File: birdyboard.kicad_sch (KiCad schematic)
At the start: 5 parts, among them SW1 SW_SPST

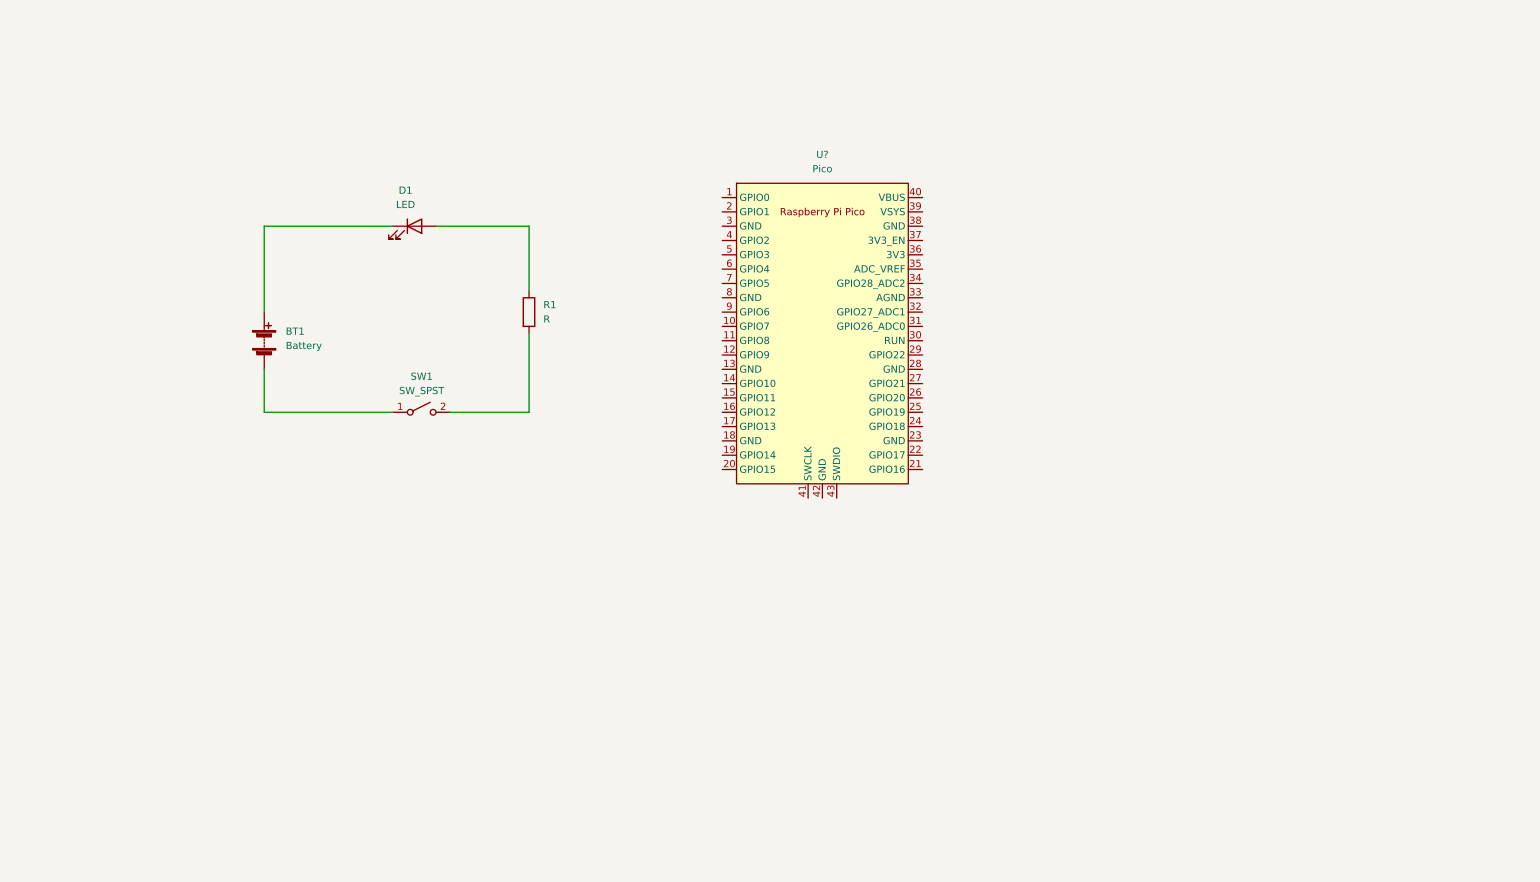
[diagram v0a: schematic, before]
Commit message: Adds footprints & symbols for RP2040 & TMC2208 boards
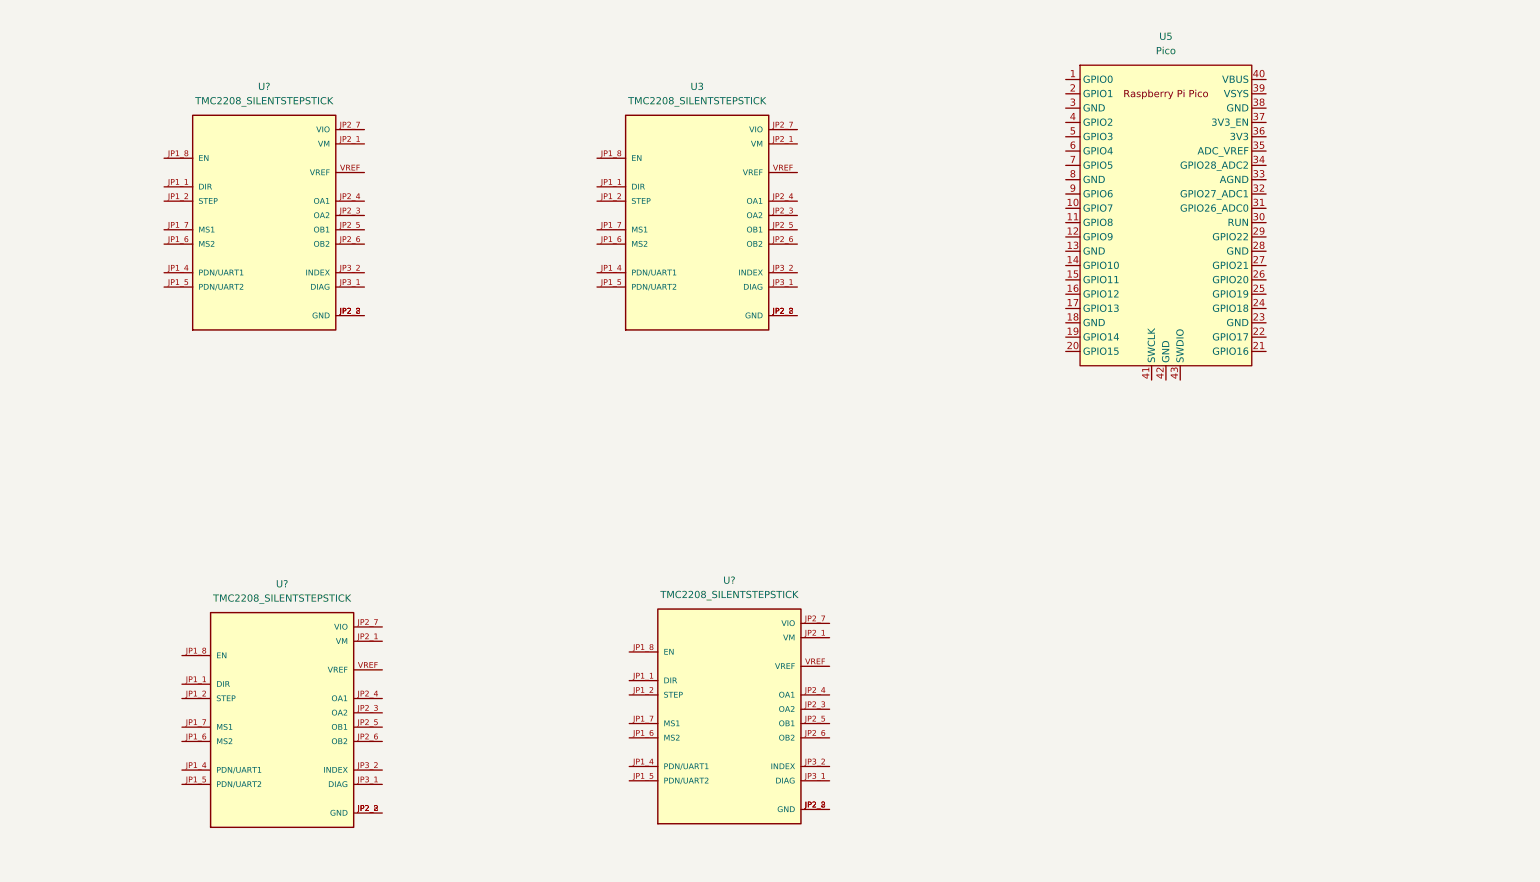
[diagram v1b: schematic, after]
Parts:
- removed BT1: Battery, symbol Device:Battery
- removed D1: LED, symbol Device:LED
- removed R1: R, symbol Device:R
- removed SW1: SW_SPST, symbol Switch:SW_SPST
- added U3, U? (x3): TMC2208_SILENTSTEPSTICK, birdyboard:TMC2208_SILENTSTEPSTICK, symbol birdyboard_library:TMC2208_SILENTSTEPSTICK
- U5: renamed from U?; footprint RPi_Pico:RPi_Pico_SMD_TH -> MCU_RaspberryPi_and_Boards:RPi_Pico_SMD_TH; symbol MCU_RaspberryPi_and_Boards:Pico -> birdyboard_library:Pico
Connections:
- new net: U3.JP2_2 (GND), U3.JP2_8 (GND)
- new net: U?.JP2_2 (GND), U?.JP2_8 (GND) (x3)
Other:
- moved on the sheet: U5
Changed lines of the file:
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@@
 (kicad_sch (version 20211123) (generator eeschema)
   (paper "A4")
-  (wire (pts (xy 109.22 60.96) (xy 109.22 72.39))
-    (stroke (width 0) (type default) (color 0 0 0 0))
-  )
-  (wire (pts (xy 109.22 80.01) (xy 109.22 93.98))
-    (stroke (width 0) (type default) (color 0 0 0 0))
-  )
-  (wire (pts (xy 62.23 93.98) (xy 62.23 86.36))
-    (stroke (width 0) (type default) (color 0 0 0 0))
-  )
-  (wire (pts (xy 109.22 93.98) (xy 95.25 93.98))
-    (stroke (width 0) (type default) (color 0 0 0 0))
-  )
-  (wire (pts (xy 62.23 60.96) (xy 85.09 60.96))
-    (stroke (width 0) (type default) (color 0 0 0 0))
-  )
-  (wire (pts (xy 92.71 60.96) (xy 109.22 60.96))
-    (stroke (width 0) (type default) (color 0 0 0 0))
-  )
-  (wire (pts (xy 62.23 76.2) (xy 62.23 60.96))
-    (stroke (width 0) (type default) (color 0 0 0 0))
-  )
-  (wire (pts (xy 85.09 93.98) (xy 62.23 93.98))
-    (stroke (width 0) (type default) (color 0 0 0 0))
-  )
-  (symbol (lib_id "Device:R") (at 109.22 76.2 0) (unit 1)
-    (in_bom yes) (on_board yes) (fields_autoplaced)
-    (property "Reference" "R1" (id 0) (at 111.76 74.9299 0)
-      (effects (font (size 1.27 1.27)) (justify left))
-    )
-    (property "Value" "R" (id 1) (at 111.76 77.4699 0)
-      (effects (font (size 1.27 1.27)) (justify left))
-    )
-    (property "Footprint" "" (id 2) (at 107.442 76.2 90)
+  (symbol (lib_id "birdyboard_library:TMC2208_SILENTSTEPSTICK") (at 139.065 59.055 0) (unit 1)
+    (in_bom yes) (on_board yes) (fields_autoplaced)
+    (property "Reference" "U3" (id 0) (at 139.065 36.195 0))
+    (property "Value" "TMC2208_SILENTSTEPSTICK" (id 1) (at 139.065 38.735 0))
+    (property "Footprint" "birdyboard:TMC2208_SILENTSTEPSTICK" (id 2) (at 139.065 59.055 0)
+      (effects (font (size 1.27 1.27)) (justify left bottom) hide)
+    )
+    (property "Datasheet" "" (id 3) (at 139.065 59.055 0)
+      (effects (font (size 1.27 1.27)) (justify left bottom) hide)
+    )
+    (property "MANUFACTURER" "Trinamic Motion" (id 4) (at 139.065 59.055 0)
+      (effects (font (size 1.27 1.27)) (justify left bottom) hide)
+    )
+    (pin "JP1_1")
+    (pin "JP1_2")
+    (pin "JP1_4")
+    (pin "JP1_5")
+    (pin "JP1_6")
+    (pin "JP1_7")
+    (pin "JP1_8")
+    (pin "JP2_1")
+    (pin "JP2_2")
+    (pin "JP2_3")
+    (pin "JP2_4")
+    (pin "JP2_5")
+    (pin "JP2_6")
+    (pin "JP2_7")
+    (pin "JP2_8")
+    (pin "JP3_1")
+    (pin "JP3_2")
+    (pin "VREF")
+  )
+  (symbol (lib_id "birdyboard_library:TMC2208_SILENTSTEPSTICK") (at 65.405 147.32 0) (unit 1)
+    (in_bom yes) (on_board yes) (fields_autoplaced)
+    (property "Reference" "U?" (id 0) (at 65.405 124.46 0))
+    (property "Value" "TMC2208_SILENTSTEPSTICK" (id 1) (at 65.405 127 0))
+    (property "Footprint" "birdyboard:TMC2208_SILENTSTEPSTICK" (id 2) (at 65.405 147.32 0)
+      (effects (font (size 1.27 1.27)) (justify left bottom) hide)
+    )
+    (property "Datasheet" "" (id 3) (at 65.405 147.32 0)
+      (effects (font (size 1.27 1.27)) (justify left bottom) hide)
+    )
+    (property "MANUFACTURER" "Trinamic Motion" (id 4) (at 65.405 147.32 0)
+      (effects (font (size 1.27 1.27)) (justify left bottom) hide)
+    )
+    (pin "JP1_1")
+    (pin "JP1_2")
+    (pin "JP1_4")
+    (pin "JP1_5")
+    (pin "JP1_6")
+    (pin "JP1_7")
+    (pin "JP1_8")
+    (pin "JP2_1")
+    (pin "JP2_2")
+    (pin "JP2_3")
+    (pin "JP2_4")
+    (pin "JP2_5")
+    (pin "JP2_6")
+    (pin "JP2_7")
+    (pin "JP2_8")
+    (pin "JP3_1")
+    (pin "JP3_2")
+    (pin "VREF")
+  )
+  (symbol (lib_id "birdyboard_library:Pico") (at 222.25 59.055 0) (unit 1)
+    (in_bom yes) (on_board yes) (fields_autoplaced)
+    (property "Reference" "U5" (id 0) (at 222.25 27.305 0))
+    (property "Value" "Pico" (id 1) (at 222.25 29.845 0))
+    (property "Footprint" "MCU_RaspberryPi_and_Boards:RPi_Pico_SMD_TH" (id 2) (at 222.25 59.055 90)
       (effects (font (size 1.27 1.27)) hide)
     )
-    (property "Datasheet" "~" (id 3) (at 109.22 76.2 0)
-      (effects (font (size 1.27 1.27)) hide)
-    )
-    (pin "1")
-    (pin "2")
-  )
-  (symbol (lib_id "Switch:SW_SPST") (at 90.17 93.98 0) (unit 1)
-    (in_bom yes) (on_board yes) (fields_autoplaced)
-    (property "Reference" "SW1" (id 0) (at 90.17 87.63 0))
-    (property "Value" "SW_SPST" (id 1) (at 90.17 90.17 0))
-    (property "Footprint" "" (id 2) (at 90.17 93.98 0)
-      (effects (font (size 1.27 1.27)) hide)
-    )
-    (property "Datasheet" "~" (id 3) (at 90.17 93.98 0)
-      (effects (font (size 1.27 1.27)) hide)
-    )
-    (pin "1")
-    (pin "2")
-  )
-  (symbol (lib_id "MCU_RaspberryPi_and_Boards:Pico") (at 161.29 80.01 0) (unit 1)
-    (in_bom yes) (on_board yes) (fields_autoplaced)
-    (property "Reference" "U?" (id 0) (at 161.29 48.26 0))
-    (property "Value" "Pico" (id 1) (at 161.29 50.8 0))
-    (property "Footprint" "RPi_Pico:RPi_Pico_SMD_TH" (id 2) (at 161.29 80.01 90)
-      (effects (font (size 1.27 1.27)) hide)
-    )
-    (property "Datasheet" "" (id 3) (at 161.29 80.01 0)
+    (property "Datasheet" "" (id 3) (at 222.25 59.055 0)
       (effects (font (size 1.27 1.27)) hide)
     )
@@
     (pin "9")
   )
-  (symbol (lib_id "Device:Battery") (at 62.23 81.28 0) (unit 1)
-    (in_bom yes) (on_board yes) (fields_autoplaced)
-    (property "Reference" "BT1" (id 0) (at 66.04 79.6289 0)
-      (effects (font (size 1.27 1.27)) (justify left))
-    )
-    (property "Value" "Battery" (id 1) (at 66.04 82.1689 0)
-      (effects (font (size 1.27 1.27)) (justify left))
-    )
-    (property "Footprint" "" (id 2) (at 62.23 79.756 90)
-      (effects (font (size 1.27 1.27)) hide)
-    )
-    (property "Datasheet" "~" (id 3) (at 62.23 79.756 90)
-      (effects (font (size 1.27 1.27)) hide)
-    )
-    (pin "1")
-    (pin "2")
-  )
-  (symbol (lib_id "Device:LED") (at 88.9 60.96 0) (unit 1)
-    (in_bom yes) (on_board yes) (fields_autoplaced)
-    (property "Reference" "D1" (id 0) (at 87.3125 54.61 0))
-    (property "Value" "LED" (id 1) (at 87.3125 57.15 0))
-    (property "Footprint" "" (id 2) (at 88.9 60.96 0)
-      (effects (font (size 1.27 1.27)) hide)
-    )
-    (property "Datasheet" "~" (id 3) (at 88.9 60.96 0)
-      (effects (font (size 1.27 1.27)) hide)
-    )
-    (pin "1")
-    (pin "2")
+  (symbol (lib_id "birdyboard_library:TMC2208_SILENTSTEPSTICK") (at 62.23 59.055 0) (unit 1)
+    (in_bom yes) (on_board yes) (fields_autoplaced)
+    (property "Reference" "U?" (id 0) (at 62.23 36.195 0))
+    (property "Value" "TMC2208_SILENTSTEPSTICK" (id 1) (at 62.23 38.735 0))
+    (property "Footprint" "birdyboard:TMC2208_SILENTSTEPSTICK" (id 2) (at 62.23 59.055 0)
+      (effects (font (size 1.27 1.27)) (justify left bottom) hide)
+    )
+    (property "Datasheet" "" (id 3) (at 62.23 59.055 0)
+      (effects (font (size 1.27 1.27)) (justify left bottom) hide)
+    )
+    (property "MANUFACTURER" "Trinamic Motion" (id 4) (at 62.23 59.055 0)
+      (effects (font (size 1.27 1.27)) (justify left bottom) hide)
+    )
+    (pin "JP1_1")
+    (pin "JP1_2")
+    (pin "JP1_4")
+    (pin "JP1_5")
+    (pin "JP1_6")
+    (pin "JP1_7")
+    (pin "JP1_8")
+    (pin "JP2_1")
+    (pin "JP2_2")
+    (pin "JP2_3")
+    (pin "JP2_4")
+    (pin "JP2_5")
+    (pin "JP2_6")
+    (pin "JP2_7")
+    (pin "JP2_8")
+    (pin "JP3_1")
+    (pin "JP3_2")
+    (pin "VREF")
+  )
+  (symbol (lib_id "birdyboard_library:TMC2208_SILENTSTEPSTICK") (at 144.78 146.685 0) (unit 1)
+    (in_bom yes) (on_board yes) (fields_autoplaced)
+    (property "Reference" "U?" (id 0) (at 144.78 123.825 0))
+    (property "Value" "TMC2208_SILENTSTEPSTICK" (id 1) (at 144.78 126.365 0))
+    (property "Footprint" "birdyboard:TMC2208_SILENTSTEPSTICK" (id 2) (at 144.78 146.685 0)
+      (effects (font (size 1.27 1.27)) (justify left bottom) hide)
+    )
+    (property "Datasheet" "" (id 3) (at 144.78 146.685 0)
+      (effects (font (size 1.27 1.27)) (justify left bottom) hide)
+    )
+    (property "MANUFACTURER" "Trinamic Motion" (id 4) (at 144.78 146.685 0)
+      (effects (font (size 1.27 1.27)) (justify left bottom) hide)
+    )
+    (pin "JP1_1")
+    (pin "JP1_2")
+    (pin "JP1_4")
+    (pin "JP1_5")
+    (pin "JP1_6")
+    (pin "JP1_7")
+    (pin "JP1_8")
+    (pin "JP2_1")
+    (pin "JP2_2")
+    (pin "JP2_3")
+    (pin "JP2_4")
+    (pin "JP2_5")
+    (pin "JP2_6")
+    (pin "JP2_7")
+    (pin "JP2_8")
+    (pin "JP3_1")
+    (pin "JP3_2")
+    (pin "VREF")
   )
   (sheet_instances
@@
   )
   (symbol_instances
-    (path "/aedc3f1a-5f87-4220-98d6-0029cc91b251"
-      (reference "BT1") (unit 1) (value "Battery") (footprint "")
-    )
-    (path "/c3e8f1bc-18b8-41bb-a51a-01d7b3e97bb6"
-      (reference "D1") (unit 1) (value "LED") (footprint "")
-    )
-    (path "/1eb82765-928c-4811-99fb-9d1e0bb48f4a"
-      (reference "R1") (unit 1) (value "R") (footprint "")
-    )
-    (path "/2680e73b-535d-4b0b-9ae2-b614fb3ffd1d"
-      (reference "SW1") (unit 1) (value "SW_SPST") (footprint "")
+    (path "/1b7241dd-50c0-4ea4-b9e4-398fecb92930"
+      (reference "U3") (unit 1) (value "TMC2208_SILENTSTEPSTICK") (footprint "birdyboard:TMC2208_SILENTSTEPSTICK")
     )
     (path "/5c28b9b9-20a8-48b6-ba53-d717d342083f"
-      (reference "U?") (unit 1) (value "Pico") (footprint "RPi_Pico:RPi_Pico_SMD_TH")
-    )
-  )
+      (reference "U5") (unit 1) (value "Pico") (footprint "MCU_RaspberryPi_and_Boards:RPi_Pico_SMD_TH")
+    )
+    (path "/344822b8-0c78-4832-98d5-254b8b20341d"
+      (reference "U?") (unit 1) (value "TMC2208_SILENTSTEPSTICK") (footprint "birdyboard:TMC2208_SILENTSTEPSTICK")
+    )
+    (path "/c5ba89e5-abf6-44af-8c5f-769135662d59"
+      (reference "U?") (unit 1) (value "TMC2208_SILENTSTEPSTICK") (footprint "birdyboard:TMC2208_SILENTSTEPSTICK")
+    )
+    (path "/f64ad3d7-b9b7-403e-af6d-671c637d8a55"
+      (reference "U?") (unit 1) (value "TMC2208_SILENTSTEPSTICK") (footprint "birdyboard:TMC2208_SILENTSTEPSTICK")
+    )
+  )
